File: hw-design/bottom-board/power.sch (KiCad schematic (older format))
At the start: 30 parts, among them J1 Power Jack, P1 HMI_POWER, U1 MURATA 5V, U2 NCP1117-5.0_TO252, U3 NCP1117-3.3_TO252, U4 LM27762

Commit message: bottom,sch: rename MPN1 to MPN
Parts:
- C1, C3: MPN (none) -> ESK228M025AL4AA; MPN1 ESK228M025AL4AA -> (none)
- C10, C13, C14, C5, C6, C7, C8: MPN (none) -> CL10A106MQ8NNNC; MPN1 CL10A106MQ8NNNC -> (none)
- C11, C9: MPN (none) -> CL10B105KP8NNNC; MPN1 CL10B105KP8NNNC -> (none)
- C12: MPN (none) -> CL10A475KP8NNNC; MPN1 CL10A475KP8NNNC -> (none)
- C2, C4: MPN (none) -> CL21A106KOFNNNE; MPN1 CL21A106KOFNNNE -> (none)
- D1, D2: MPN (none) -> MBR230LSFT1G; MPN1 MBR230LSFT1G -> (none)
- R1: MPN (none) -> RR0816P-103-D; MPN1 RR0816P-103-D -> (none)
- R2, R3: MPN (none) -> RR0816P-3163-D-49D; MPN1 RR0816P-3163-D-49D -> (none)
- R4, R5: MPN (none) -> RR0816P-104-D; MPN1 RR0816P-104-D -> (none)
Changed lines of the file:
@@
 F 2 "Diode_SMD:D_SOD-123F" H 3350 1950 50  0001 C CNN
 F 3 "" H 3350 1950 50  0001 C CNN
-F 4 "MBR230LSFT1G" H 500 -600 50  0001 C CNN "MPN1"
+F 4 "MBR230LSFT1G" H 500 -600 50  0001 C CNN "MPN"
 F 5 "MBR230S1F-7" H 3350 1950 50  0001 C CNN "MPN2"
 F 6 "DB2W31800L" H 3350 1950 50  0001 C CNN "MPN3"
@@
 F 2 "Capacitor_THT:CP_Radial_D13.0mm_P5.00mm" H 3738 2000 30  0001 C CNN
 F 3 "" H 3700 2150 60  0000 C CNN
-F 4 "ESK228M025AL4AA" H 200 -650 50  0001 C CNN "MPN1"
+F 4 "ESK228M025AL4AA" H 200 -650 50  0001 C CNN "MPN"
 F 5 "ECA-1EM222" H 3700 2150 50  0001 C CNN "MPN2"
 	1    3700 2150
@@
 F 2 "Capacitor_THT:CP_Radial_D13.0mm_P5.00mm" H 4338 2000 30  0001 C CNN
 F 3 "" H 4300 2150 60  0000 C CNN
-F 4 "ESK228M025AL4AA" H 0   0   50  0001 C CNN "MPN1"
+F 4 "ESK228M025AL4AA" H 0   0   50  0001 C CNN "MPN"
 F 5 "ECA-1EM222" H 0   0   50  0001 C CNN "MPN2"
 	1    4300 2150
@@
 F 2 "Resistor_SMD:R_0603_1608Metric" H 7800 2150 50  0001 C CNN
 F 3 "" H 7800 2150 50  0001 C CNN
-F 4 "RR0816P-103-D" V 7800 2150 60  0001 C CNN "MPN1"
+F 4 "RR0816P-103-D" V 7800 2150 60  0001 C CNN "MPN"
 F 5 "RT0603DRE0710KL" V 7800 2150 50  0001 C CNN "MPN2"
 F 6 "RJ-PB3D1002V" V 7800 2150 50  0001 C CNN "MPN3"
@@
 F 2 "Resistor_SMD:R_0603_1608Metric" H 9050 2050 50  0001 C CNN
 F 3 "" H 9050 2050 50  0001 C CNN
-F 4 "RR0816P-3163-D-49D" V 9050 2050 60  0001 C CNN "MPN1"
+F 4 "RR0816P-3163-D-49D" V 9050 2050 60  0001 C CNN "MPN"
 F 5 "RC0603FR-07316KL" V 9050 2050 50  0001 C CNN "MPN2"
 F 6 "ERJ-3EKF3163V" V 9050 2050 50  0001 C CNN "MPN3"
@@
 F 2 "Resistor_SMD:R_0603_1608Metric" H 9300 2150 50  0001 C CNN
 F 3 "" H 9300 2150 50  0001 C CNN
-F 4 "RR0816P-104-D" V 9300 2150 60  0001 C CNN "MPN1"
+F 4 "RR0816P-104-D" V 9300 2150 60  0001 C CNN "MPN"
 F 5 "RT0603DRE07100KL" V 9300 2150 50  0001 C CNN "MPN2"
 F 6 "ERJ-PB3D1003V" V 9300 2150 50  0001 C CNN "MPN3"
@@
 F 2 "Capacitor_SMD:C_0603_1608Metric" H 8950 2950 60  0001 C CNN
 F 3 "" H 8950 2950 60  0000 C CNN
-F 4 "CL10A475KP8NNNC" H 4750 1950 50  0001 C CNN "MPN1"
+F 4 "CL10A475KP8NNNC" H 4750 1950 50  0001 C CNN "MPN"
 F 5 "CL10B475KQ8NQNC" H 8950 2950 50  0001 C CNN "MPN2"
 	1    8950 2950
@@
 F 2 "Capacitor_SMD:C_0603_1608Metric" H 7000 2150 60  0001 C CNN
 F 3 "" H 7000 2150 60  0000 C CNN
-F 4 "CL10B105KP8NNNC" H 2800 1150 50  0001 C CNN "MPN1"
+F 4 "CL10B105KP8NNNC" H 2800 1150 50  0001 C CNN "MPN"
 F 5 "GRM188R60J105KA01D" V 7000 2150 50  0001 C CNN "MPN2"
 	1    7000 2150
@@
 F 2 "Capacitor_SMD:C_0805_2012Metric" H 4200 3900 60  0001 C CNN
 F 3 "" H 4200 3900 60  0000 C CNN
-F 4 "CL21A106KOFNNNE" H -1100 -1450 50  0001 C CNN "MPN1"
+F 4 "CL21A106KOFNNNE" H -1100 -1450 50  0001 C CNN "MPN"
 F 5 "C2012X5R1C106M085AC" H 4200 3900 50  0001 C CNN "MPN2"
 	1    4200 3900
@@
 F 2 "Capacitor_SMD:C_0805_2012Metric" H 5000 2150 60  0001 C CNN
 F 3 "" H 5000 2150 60  0000 C CNN
-F 4 "CL21A106KOFNNNE" H -300 -3200 50  0001 C CNN "MPN1"
+F 4 "CL21A106KOFNNNE" H -300 -3200 50  0001 C CNN "MPN"
 F 5 "C2012X5R1C106M085AC" H 5000 2150 50  0001 C CNN "MPN2"
 	1    5000 2150
@@
 F 2 "Capacitor_SMD:C_0603_1608Metric" H 5900 2150 60  0001 C CNN
 F 3 "" H 5900 2150 60  0000 C CNN
-F 4 "CL10A106MQ8NNNC" H 600 -3200 50  0001 C CNN "MPN1"
+F 4 "CL10A106MQ8NNNC" H 600 -3200 50  0001 C CNN "MPN"
 F 5 "GRM188R60J106KE47D" H 5900 2150 50  0001 C CNN "MPN2"
 F 6 "CC0603MRX5R5BB106" V 5900 2150 50  0001 C CNN "MPN3"
@@
 F 2 "Capacitor_SMD:C_0603_1608Metric" H 7350 2150 60  0001 C CNN
 F 3 "" H 7350 2150 60  0000 C CNN
-F 4 "CL10A106MQ8NNNC" H 2050 -3200 50  0001 C CNN "MPN1"
+F 4 "CL10A106MQ8NNNC" H 2050 -3200 50  0001 C CNN "MPN"
 F 5 "GRM188R60J106KE47D" H 7350 2150 50  0001 C CNN "MPN2"
 F 6 "CC0603MRX5R5BB106" V 7350 2150 50  0001 C CNN "MPN3"
@@
 F 2 "Capacitor_SMD:C_0603_1608Metric" H 7850 2650 60  0001 C CNN
 F 3 "" H 7850 2650 60  0000 C CNN
-F 4 "CL10B105KP8NNNC" H 3650 1650 50  0001 C CNN "MPN1"
+F 4 "CL10B105KP8NNNC" H 3650 1650 50  0001 C CNN "MPN"
 F 5 "GRM188R60J105KA01D" V 7850 2650 50  0001 C CNN "MPN2"
 	1    7850 2650
@@
 F 2 "Resistor_SMD:R_0603_1608Metric" H 9050 2450 50  0001 C CNN
 F 3 "" H 9050 2450 50  0001 C CNN
-F 4 "RR0816P-3163-D-49D" V 9050 2450 60  0001 C CNN "MPN1"
+F 4 "RR0816P-3163-D-49D" V 9050 2450 60  0001 C CNN "MPN"
 F 5 "RC0603FR-07316KL" V 9050 2450 50  0001 C CNN "MPN2"
 F 6 "ERJ-3EKF3163V" V 9050 2450 50  0001 C CNN "MPN3"
@@
 F 2 "Resistor_SMD:R_0603_1608Metric" H 9300 2350 50  0001 C CNN
 F 3 "" H 9300 2350 50  0001 C CNN
-F 4 "RR0816P-104-D" V 9300 2350 60  0001 C CNN "MPN1"
+F 4 "RR0816P-104-D" V 9300 2350 60  0001 C CNN "MPN"
 F 5 "RT0603DRE07100KL" V 9300 2350 50  0001 C CNN "MPN2"
 F 6 "ERJ-PB3D1003V" V 9300 2350 50  0001 C CNN "MPN3"
@@
 F 2 "Capacitor_SMD:C_0603_1608Metric" H 9650 2050 60  0001 C CNN
 F 3 "" H 9650 2050 60  0000 C CNN
-F 4 "CL10A106MQ8NNNC" H 4350 -3300 50  0001 C CNN "MPN1"
+F 4 "CL10A106MQ8NNNC" H 4350 -3300 50  0001 C CNN "MPN"
 F 5 "GRM188R60J106KE47D" H 9650 2050 50  0001 C CNN "MPN2"
 F 6 "CC0603MRX5R5BB106" V 9650 2050 50  0001 C CNN "MPN3"
@@
 F 2 "Capacitor_SMD:C_0603_1608Metric" H 9650 2450 60  0001 C CNN
 F 3 "" H 9650 2450 60  0000 C CNN
-F 4 "CL10A106MQ8NNNC" H 4350 -2900 50  0001 C CNN "MPN1"
+F 4 "CL10A106MQ8NNNC" H 4350 -2900 50  0001 C CNN "MPN"
 F 5 "GRM188R60J106KE47D" H 9650 2450 50  0001 C CNN "MPN2"
 F 6 "CC0603MRX5R5BB106" V 9650 2450 50  0001 C CNN "MPN3"
@@
 F 2 "Capacitor_SMD:C_0603_1608Metric" H 5200 3900 60  0001 C CNN
 F 3 "" H 5200 3900 60  0000 C CNN
-F 4 "CL10A106MQ8NNNC" H -100 -1450 50  0001 C CNN "MPN1"
+F 4 "CL10A106MQ8NNNC" H -100 -1450 50  0001 C CNN "MPN"
 F 5 "GRM188R60J106KE47D" H 5200 3900 50  0001 C CNN "MPN2"
 F 6 "CC0603MRX5R5BB106" V 5200 3900 50  0001 C CNN "MPN3"
@@
 F 2 "Capacitor_SMD:C_0603_1608Metric" H 5900 3900 60  0001 C CNN
 F 3 "" H 5900 3900 60  0000 C CNN
-F 4 "CL10A106MQ8NNNC" H 600 -1450 50  0001 C CNN "MPN1"
+F 4 "CL10A106MQ8NNNC" H 600 -1450 50  0001 C CNN "MPN"
 F 5 "GRM188R60J106KE47D" H 5900 3900 50  0001 C CNN "MPN2"
 F 6 "CC0603MRX5R5BB106" V 5900 3900 50  0001 C CNN "MPN3"
@@
 F 2 "Capacitor_SMD:C_0603_1608Metric" H 6800 3900 60  0001 C CNN
 F 3 "" H 6800 3900 60  0000 C CNN
-F 4 "CL10A106MQ8NNNC" H 1500 -1450 50  0001 C CNN "MPN1"
+F 4 "CL10A106MQ8NNNC" H 1500 -1450 50  0001 C CNN "MPN"
 F 5 "GRM188R60J106KE47D" H 6800 3900 50  0001 C CNN "MPN2"
 F 6 "CC0603MRX5R5BB106" V 6800 3900 50  0001 C CNN "MPN3"
@@
 F 2 "Diode_SMD:D_SOD-123F" H 3350 3700 50  0001 C CNN
 F 3 "" H 3350 3700 50  0001 C CNN
-F 4 "MBR230LSFT1G" H 500 1150 50  0001 C CNN "MPN1"
+F 4 "MBR230LSFT1G" H 500 1150 50  0001 C CNN "MPN"
 F 5 "MBR230S1F-7" H 3350 3700 50  0001 C CNN "MPN2"
 F 6 "DB2W31800L" H 3350 3700 50  0001 C CNN "MPN3"

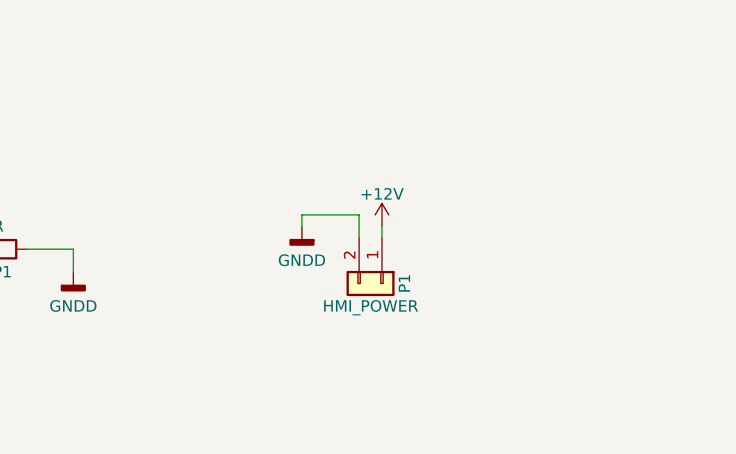
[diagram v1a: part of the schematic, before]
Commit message: bottom,sch: annotate schematic symbols again
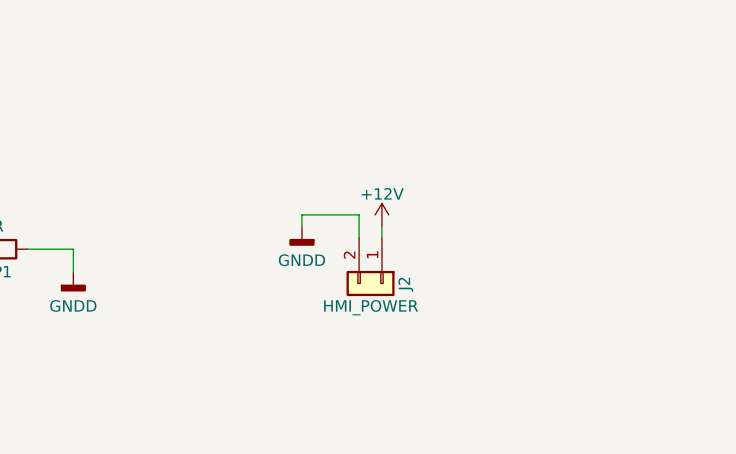
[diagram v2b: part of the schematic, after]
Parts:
- renumbered P1 to J2
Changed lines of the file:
@@
 $EndComp
 $Comp
-L Connector_Generic:Conn_01x02 P1
+L Connector_Generic:Conn_01x02 J2
 U 1 1 5B572324
 P 8750 5550
-F 0 "P1" H 8750 5650 50  0000 C CNN
+F 0 "J2" H 8750 5650 50  0000 C CNN
 F 1 "HMI_POWER" V 8850 5500 50  0000 C CNN
 F 2 "footprints:B2B-XH-A" H 8750 5550 50  0001 C CNN

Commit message: bottom,sch: update murata footprint
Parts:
- U1: footprint Package_TO_SOT_THT:TO-220-3_Vertical -> footprints:OKI-78SR_Vertical
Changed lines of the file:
@@
 F 0 "U1" H 4650 3900 50  0000 C CNN
 F 1 "MURATA 5V" H 4450 3825 50  0000 L CNN
-F 2 "Package_TO_SOT_THT:TO-220-3_Vertical" H 4650 3925 50  0001 C CIN
+F 2 "footprints:OKI-78SR_Vertical" H 4650 3925 50  0001 C CIN
 F 3 "https://power.murata.com/data/power/oki-78sr.pdf" H 4650 3650 50  0001 C CNN
 F 4 "OKI-78SR-5/1.5-W36-C" H 4650 3700 60  0001 C CNN "MPN"

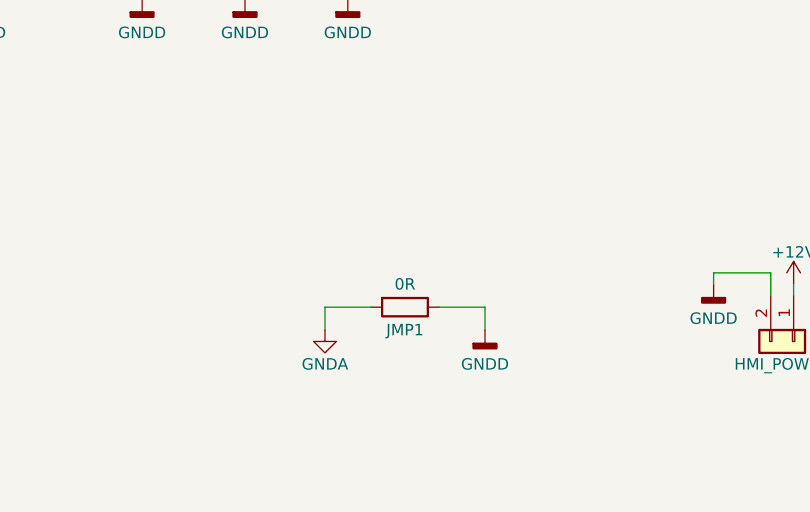
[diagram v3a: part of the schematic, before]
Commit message: bottom: [wip] connecting power traces
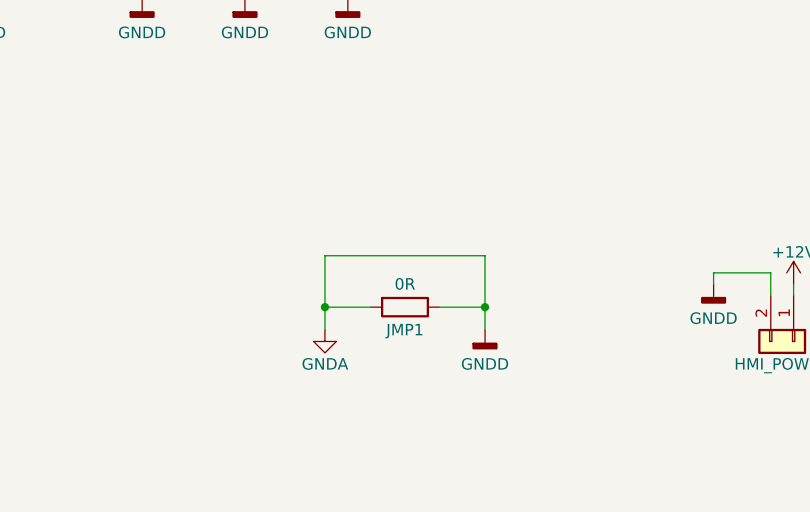
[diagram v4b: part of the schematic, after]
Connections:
- wire segments 105 -> 108
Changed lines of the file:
@@
 	-1   0    0    1
 $EndComp
+Wire Wire Line
+	6700 5400 6700 5175
+Wire Wire Line
+	6700 5175 7400 5175
+Wire Wire Line
+	7400 5175 7400 5400
+Connection ~ 6700 5400
+Connection ~ 7400 5400
 $EndSCHEMATC

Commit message: bottom,sch: add alternative parts for the linear regulators
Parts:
- U2: MPN NCP1117DT50 -> LD1117DT50CTR; MPN2 (none) -> NCP1117DT50
- U3: MPN NCP1117DT33 -> NCP1117DT33RKG; MPN2 (none) -> LD1086DT33TR
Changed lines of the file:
@@
 F 2 "Package_TO_SOT_SMD:TO-252-2" H 6350 3925 50  0001 C CNN
 F 3 "http://www.onsemi.com/pub_link/Collateral/NCP1117-D.PDF" H 6350 3700 50  0001 C CNN
-F 4 "NCP1117DT33" H 6350 3700 50  0001 C CNN "MPN"
+F 4 "NCP1117DT33RKG" H 6350 3700 50  0001 C CNN "MPN"
+F 5 "LD1086DT33TR" H 6350 3700 50  0001 C CNN "MPN2"
 	1    6350 3700
 	1    0    0    -1
@@
 F 2 "Package_TO_SOT_SMD:TO-252-2" H 5450 2175 50  0001 C CNN
 F 3 "http://www.onsemi.com/pub_link/Collateral/NCP1117-D.PDF" H 5450 1950 50  0001 C CNN
-F 4 "NCP1117DT50" H 5450 1950 50  0001 C CNN "MPN"
+F 4 "LD1117DT50CTR" H 5450 1950 50  0001 C CNN "MPN"
+F 5 "NCP1117DT50" H 5450 1950 50  0001 C CNN "MPN2"
 	1    5450 1950
 	1    0    0    -1

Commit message: bottom,sch: many fixes and addition of test points
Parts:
- removed C10, C13, C14: 10uF, Capacitor_SMD:C_0603_1608Metric, symbol Device:C_Small
- removed C11, C9: 1uF, Capacitor_SMD:C_0603_1608Metric, symbol Device:C_Small
- removed C12: 4.7uF, Capacitor_SMD:C_0603_1608Metric, symbol Device:C_Small
- removed R1: 10k 1%, Resistor_SMD:R_0603_1608Metric, symbol Device:R_Small
- removed R2, R3: 316k 1%, Resistor_SMD:R_0603_1608Metric, symbol Device:R_Small
- removed R4, R5: 100k 1%, Resistor_SMD:R_0603_1608Metric, symbol Device:R_Small
- removed U2: NCP1117-5.0_TO252, Package_TO_SOT_SMD:TO-252-2, symbol Regulator_Linear:NCP1117-5.0_TO252
- removed U4: LM27762, Package_SON:WSON-12-1EP_3x2mm_P0.5mm_EP1x2.65_ThermalVias, symbol Regulator_SwitchedCapacitor:LM27762
- added TP1, TP2, TP3, TP4, TP5: TestPoint, TestPoint:TestPoint_Pad_D1.0mm, symbol Connector:TestPoint
- added U2: LD1117S50TR_SOT223, Package_TO_SOT_SMD:SOT-223-3_TabPin2, symbol Regulator_Linear:LD1117S50TR_SOT223
- F1: value Fuse -> Fuse 2A
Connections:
- net labels removed: -5VA
- wire segments 108 -> 74
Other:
- note removed: "Read LM27762DSST datasheet and evaluation board\nuser's guide for layout instructions and reference"

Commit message: bottom,sch: replace 3.3V regulator
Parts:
- removed C7, C8: 10uF, Capacitor_SMD:C_0603_1608Metric, symbol Device:C_Small
- removed TP5: TestPoint, TestPoint:TestPoint_Pad_D1.0mm, symbol Connector:TestPoint
- removed U3: NCP1117-3.3_TO252, Package_TO_SOT_SMD:TO-252-2, symbol Regulator_Linear:NCP1117-3.3_TO252
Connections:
- net labels removed: +3.3V
- wire segments 74 -> 63
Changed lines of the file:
@@
 	1    0    0    -1
 $EndComp
-Text Notes 4250 1450 2    100  ~ 0
+Text Notes 4875 1450 2    100  ~ 0
 Analog
 $Comp
@@
 $EndComp
 $Comp
-L power:GNDD #PWR020
-U 1 1 5B4FCD6C
-P 5900 4050
-F 0 "#PWR020" H 5900 3800 50  0001 C CNN
-F 1 "GNDD" H 5900 3900 50  0000 C CNN
-F 2 "" H 5900 4050 60  0000 C CNN
-F 3 "" H 5900 4050 60  0000 C CNN
-	1    5900 4050
-	1    0    0    -1
-$EndComp
-$Comp
 L power:GNDD #PWR013
 U 1 1 5B4FCD72
@@
 	4950 3700 5200 3700
 Connection ~ 3750 3700
-Wire Wire Line
-	5900 4000 5900 4050
-Wire Wire Line
-	5900 3800 5900 3700
 $Comp
 L power:+5VD #PWR018
@@
 $EndComp
 $Comp
-L power:GNDD #PWR021
-U 1 1 5B5A8814
-P 6350 4050
-F 0 "#PWR021" H 6350 3800 50  0001 C CNN
-F 1 "GNDD" H 6350 3900 50  0000 C CNN
-F 2 "" H 6350 4050 60  0000 C CNN
-F 3 "" H 6350 4050 60  0000 C CNN
-	1    6350 4050
-	1    0    0    -1
-$EndComp
-Wire Wire Line
-	6350 4000 6350 4050
-Connection ~ 5900 3700
-$Comp
 L power:GNDD #PWR016
 U 1 1 5B5AA612
@@
 Wire Wire Line
 	5200 3800 5200 3700
-$Comp
-L power:GNDD #PWR023
-U 1 1 5B5AABDF
-P 6800 4050
-F 0 "#PWR023" H 6800 3800 50  0001 C CNN
-F 1 "GNDD" H 6800 3900 50  0000 C CNN
-F 2 "" H 6800 4050 60  0000 C CNN
-F 3 "" H 6800 4050 60  0000 C CNN
-	1    6800 4050
-	1    0    0    -1
-$EndComp
-Wire Wire Line
-	6800 4000 6800 4050
-Wire Wire Line
-	6800 3800 6800 3700
-$Comp
-L power:+3.3V #PWR025
-U 1 1 5B5ABE4B
-P 7100 3550
-F 0 "#PWR025" H 7100 3400 50  0001 C CNN
-F 1 "+3.3V" H 7100 3690 50  0000 C CNN
-F 2 "" H 7100 3550 60  0000 C CNN
-F 3 "" H 7100 3550 60  0000 C CNN
-	1    7100 3550
-	1    0    0    -1
-$EndComp
-Wire Wire Line
-	6650 3700 6800 3700
-Wire Wire Line
-	7100 3700 7100 3550
-Connection ~ 6800 3700
 Wire Wire Line
 	5000 1950 5150 1950
@@
 Wire Wire Line
 	5550 3700 5625 3700
-Wire Wire Line
-	5900 3700 6050 3700
-Wire Wire Line
-	6800 3700 7100 3700
-$Comp
-L Regulator_Linear:NCP1117-3.3_TO252 U3
-U 1 1 5B5A279A
-P 6350 3700
-F 0 "U3" H 6350 3942 50  0000 C CNN
-F 1 "NCP1117-3.3_TO252" H 6350 3851 50  0000 C CNN
-F 2 "Package_TO_SOT_SMD:TO-252-2" H 6350 3925 50  0001 C CNN
-F 3 "http://www.onsemi.com/pub_link/Collateral/NCP1117-D.PDF" H 6350 3700 50  0001 C CNN
-F 4 "NCP1117DT33RKG" H 6350 3700 50  0001 C CNN "MPN"
-F 5 "LD1086DT33TR" H 6350 3700 50  0001 C CNN "MPN2"
-	1    6350 3700
-	1    0    0    -1
-$EndComp
 Wire Wire Line
 	2150 1950 2500 1950
@@
 F 6 "CC0603MRX5R5BB106" V 5200 3900 50  0001 C CNN "MPN3"
 	1    5200 3900
-	1    0    0    -1
-$EndComp
-$Comp
-L Device:C_Small C7
-U 1 1 5B664E36
-P 5900 3900
-F 0 "C7" V 5700 3900 50  0000 C CNN
-F 1 "10uF" V 5775 3900 50  0000 C CNN
-F 2 "Capacitor_SMD:C_0603_1608Metric" H 5900 3900 60  0001 C CNN
-F 3 "" H 5900 3900 60  0000 C CNN
-F 4 "CL10A106MQ8NNNC" H 600 -1450 50  0001 C CNN "MPN"
-F 5 "GRM188R60J106KE47D" H 5900 3900 50  0001 C CNN "MPN2"
-F 6 "CC0603MRX5R5BB106" V 5900 3900 50  0001 C CNN "MPN3"
-	1    5900 3900
-	1    0    0    -1
-$EndComp
-$Comp
-L Device:C_Small C8
-U 1 1 5B664EB2
-P 6800 3900
-F 0 "C8" V 6600 3900 50  0000 C CNN
-F 1 "10uF" V 6675 3900 50  0000 C CNN
-F 2 "Capacitor_SMD:C_0603_1608Metric" H 6800 3900 60  0001 C CNN
-F 3 "" H 6800 3900 60  0000 C CNN
-F 4 "CL10A106MQ8NNNC" H 1500 -1450 50  0001 C CNN "MPN"
-F 5 "GRM188R60J106KE47D" H 6800 3900 50  0001 C CNN "MPN2"
-F 6 "CC0603MRX5R5BB106" V 6800 3900 50  0001 C CNN "MPN3"
-	1    6800 3900
 	1    0    0    -1
 $EndComp
@@
 	1    0    0    -1
 $EndComp
-Connection ~ 5625 3700
-Wire Wire Line
-	5625 3700 5900 3700
-$Comp
-L Connector:TestPoint TP5
-U 1 1 5BDAECF6
-P 7175 3700
-F 0 "TP5" H 7233 3774 50  0000 L CNN
-F 1 "TestPoint" H 7233 3729 50  0001 L CNN
-F 2 "TestPoint:TestPoint_Pad_D1.0mm" H 7375 3700 50  0001 C CNN
-F 3 "~" H 7375 3700 50  0001 C CNN
-	1    7175 3700
-	1    0    0    -1
-$EndComp
-Wire Wire Line
-	7175 3700 7100 3700
-Connection ~ 7100 3700
 $EndSCHEMATC
